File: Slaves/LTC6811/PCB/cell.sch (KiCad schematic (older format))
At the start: 5 parts

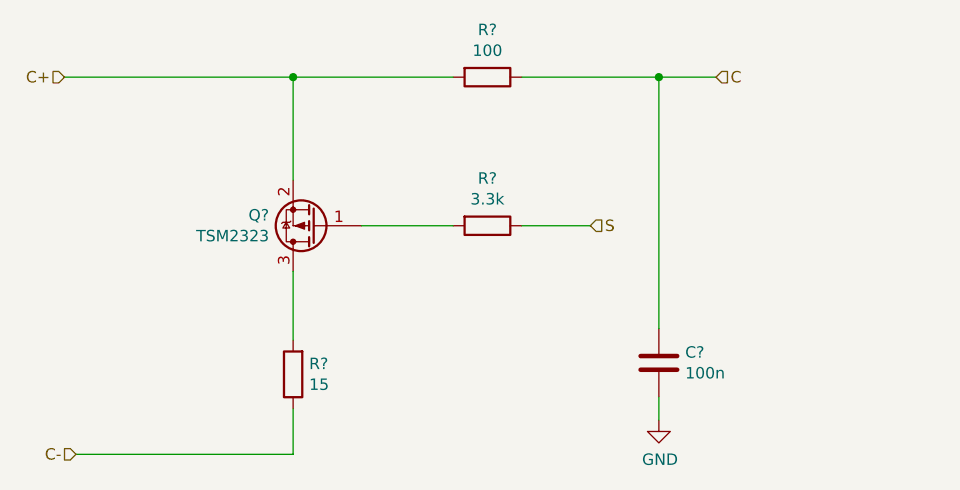
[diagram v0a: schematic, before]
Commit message: LTC6811 PCB completed
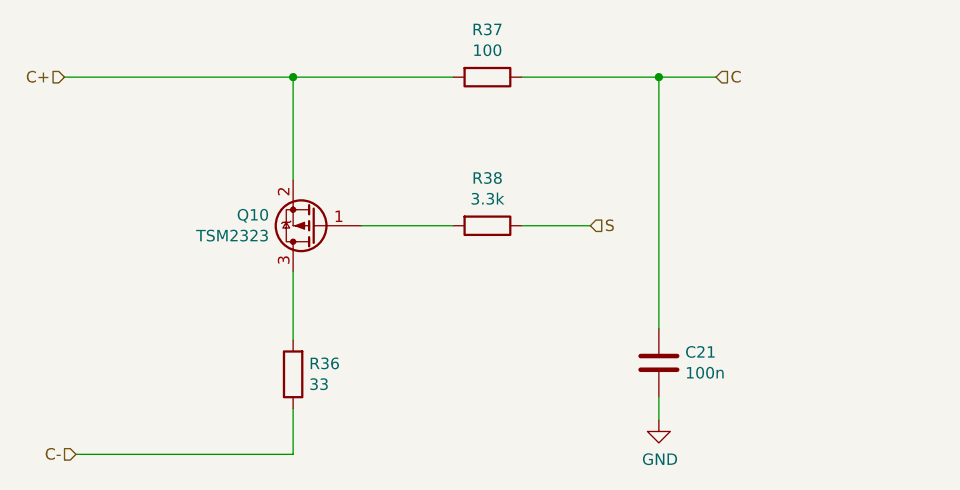
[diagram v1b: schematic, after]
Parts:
- C13: renamed from C?; footprint Capacitors_SMD:C_0805_HandSoldering -> Capacitors_SMD:C_0603_HandSoldering
- R12: renamed from R?; value 15 -> 33; footprint Resistors_SMD:R_2512_HandSoldering -> Resistors_SMD:R_2512
- gave numbers to parts that had none: 3
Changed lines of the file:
@@
 $Descr A4 11693 8268
 encoding utf-8
-Sheet 2 13
+Sheet 10 13
 Title ""
 Date ""
@@
 $EndDescr
 $Comp
-L Device:R R?
+L Device:R R13
 U 1 1 5C4F5B30
 P 4650 2700
-AR Path="/5C4F59F4/5C4F5B30" Ref="R?"  Part="1"
-AR Path="/5C4FCBE0/5C4F5B30" Ref="R?"  Part="1"
-AR Path="/5C4FCED2/5C4F5B30" Ref="R?"  Part="1"
-AR Path="/5C4FCED8/5C4F5B30" Ref="R?"  Part="1"
-AR Path="/5C4FD32A/5C4F5B30" Ref="R?"  Part="1"
-AR Path="/5C4FD330/5C4F5B30" Ref="R?"  Part="1"
-AR Path="/5C4FD336/5C4F5B30" Ref="R?"  Part="1"
-AR Path="/5C4FD33C/5C4F5B30" Ref="R?"  Part="1"
-AR Path="/5C4FFA25/5C4F5B30" Ref="R?"  Part="1"
-AR Path="/5C4FFA2B/5C4F5B30" Ref="R?"  Part="1"
-AR Path="/5C4FFA31/5C4F5B30" Ref="R?"  Part="1"
-AR Path="/5C4FFA37/5C4F5B30" Ref="R?"  Part="1"
+AR Path="/5C4F59F4/5C4F5B30" Ref="R13"  Part="1"
+AR Path="/5C4FCBE0/5C4F5B30" Ref="R16"  Part="1"
+AR Path="/5C4FCED2/5C4F5B30" Ref="R19"  Part="1"
+AR Path="/5C4FCED8/5C4F5B30" Ref="R22"  Part="1"
+AR Path="/5C4FD32A/5C4F5B30" Ref="R25"  Part="1"
+AR Path="/5C4FD330/5C4F5B30" Ref="R28"  Part="1"
+AR Path="/5C4FD336/5C4F5B30" Ref="R31"  Part="1"
+AR Path="/5C4FD33C/5C4F5B30" Ref="R34"  Part="1"
+AR Path="/5C4FFA25/5C4F5B30" Ref="R37"  Part="1"
+AR Path="/5C4FFA2B/5C4F5B30" Ref="R40"  Part="1"
+AR Path="/5C4FFA31/5C4F5B30" Ref="R43"  Part="1"
+AR Path="/5C4FFA37/5C4F5B30" Ref="R46"  Part="1"
 AR Path="/5C4FFA3D/5C4F5B30" Ref="R?"  Part="1"
 AR Path="/5C4FFA43/5C4F5B30" Ref="R?"  Part="1"
-F 0 "R?" V 4443 2700 50  0000 C CNN
+F 0 "R37" V 4443 2700 50  0000 C CNN
 F 1 "100" V 4534 2700 50  0000 C CNN
 F 2 "Resistors_SMD:R_0603_HandSoldering" V 4580 2700 50  0001 C CNN
@@
 $EndComp
 $Comp
-L Device:R R?
+L Device:R R14
 U 1 1 5C4F5DDD
 P 4650 3350
-AR Path="/5C4F59F4/5C4F5DDD" Ref="R?"  Part="1"
-AR Path="/5C4FCBE0/5C4F5DDD" Ref="R?"  Part="1"
-AR Path="/5C4FCED2/5C4F5DDD" Ref="R?"  Part="1"
-AR Path="/5C4FCED8/5C4F5DDD" Ref="R?"  Part="1"
-AR Path="/5C4FD32A/5C4F5DDD" Ref="R?"  Part="1"
-AR Path="/5C4FD330/5C4F5DDD" Ref="R?"  Part="1"
-AR Path="/5C4FD336/5C4F5DDD" Ref="R?"  Part="1"
-AR Path="/5C4FD33C/5C4F5DDD" Ref="R?"  Part="1"
-AR Path="/5C4FFA25/5C4F5DDD" Ref="R?"  Part="1"
-AR Path="/5C4FFA2B/5C4F5DDD" Ref="R?"  Part="1"
-AR Path="/5C4FFA31/5C4F5DDD" Ref="R?"  Part="1"
-AR Path="/5C4FFA37/5C4F5DDD" Ref="R?"  Part="1"
+AR Path="/5C4F59F4/5C4F5DDD" Ref="R14"  Part="1"
+AR Path="/5C4FCBE0/5C4F5DDD" Ref="R17"  Part="1"
+AR Path="/5C4FCED2/5C4F5DDD" Ref="R20"  Part="1"
+AR Path="/5C4FCED8/5C4F5DDD" Ref="R23"  Part="1"
+AR Path="/5C4FD32A/5C4F5DDD" Ref="R26"  Part="1"
+AR Path="/5C4FD330/5C4F5DDD" Ref="R29"  Part="1"
+AR Path="/5C4FD336/5C4F5DDD" Ref="R32"  Part="1"
+AR Path="/5C4FD33C/5C4F5DDD" Ref="R35"  Part="1"
+AR Path="/5C4FFA25/5C4F5DDD" Ref="R38"  Part="1"
+AR Path="/5C4FFA2B/5C4F5DDD" Ref="R41"  Part="1"
+AR Path="/5C4FFA31/5C4F5DDD" Ref="R44"  Part="1"
+AR Path="/5C4FFA37/5C4F5DDD" Ref="R47"  Part="1"
 AR Path="/5C4FFA3D/5C4F5DDD" Ref="R?"  Part="1"
 AR Path="/5C4FFA43/5C4F5DDD" Ref="R?"  Part="1"
-F 0 "R?" V 4443 3350 50  0000 C CNN
+F 0 "R38" V 4443 3350 50  0000 C CNN
 F 1 "3.3k" V 4534 3350 50  0000 C CNN
 F 2 "Resistors_SMD:R_0603_HandSoldering" V 4580 3350 50  0001 C CNN
@@
 $EndComp
 $Comp
-L Device:Q_PMOS_GSD Q?
+L Device:Q_PMOS_GSD Q2
 U 1 1 5C4F756B
 P 3900 3350
-AR Path="/5C4F59F4/5C4F756B" Ref="Q?"  Part="1"
-AR Path="/5C4FCBE0/5C4F756B" Ref="Q?"  Part="1"
-AR Path="/5C4FCED2/5C4F756B" Ref="Q?"  Part="1"
-AR Path="/5C4FCED8/5C4F756B" Ref="Q?"  Part="1"
-AR Path="/5C4FD32A/5C4F756B" Ref="Q?"  Part="1"
-AR Path="/5C4FD330/5C4F756B" Ref="Q?"  Part="1"
-AR Path="/5C4FD336/5C4F756B" Ref="Q?"  Part="1"
-AR Path="/5C4FD33C/5C4F756B" Ref="Q?"  Part="1"
-AR Path="/5C4FFA25/5C4F756B" Ref="Q?"  Part="1"
-AR Path="/5C4FFA2B/5C4F756B" Ref="Q?"  Part="1"
-AR Path="/5C4FFA31/5C4F756B" Ref="Q?"  Part="1"
-AR Path="/5C4FFA37/5C4F756B" Ref="Q?"  Part="1"
+AR Path="/5C4F59F4/5C4F756B" Ref="Q2"  Part="1"
+AR Path="/5C4FCBE0/5C4F756B" Ref="Q3"  Part="1"
+AR Path="/5C4FCED2/5C4F756B" Ref="Q4"  Part="1"
+AR Path="/5C4FCED8/5C4F756B" Ref="Q5"  Part="1"
+AR Path="/5C4FD32A/5C4F756B" Ref="Q6"  Part="1"
+AR Path="/5C4FD330/5C4F756B" Ref="Q7"  Part="1"
+AR Path="/5C4FD336/5C4F756B" Ref="Q8"  Part="1"
+AR Path="/5C4FD33C/5C4F756B" Ref="Q9"  Part="1"
+AR Path="/5C4FFA25/5C4F756B" Ref="Q10"  Part="1"
+AR Path="/5C4FFA2B/5C4F756B" Ref="Q11"  Part="1"
+AR Path="/5C4FFA31/5C4F756B" Ref="Q12"  Part="1"
+AR Path="/5C4FFA37/5C4F756B" Ref="Q13"  Part="1"
 AR Path="/5C4FFA3D/5C4F756B" Ref="Q?"  Part="1"
 AR Path="/5C4FFA43/5C4F756B" Ref="Q?"  Part="1"
-F 0 "Q?" H 4105 3304 50  0000 L CNN
+F 0 "Q10" H 4105 3304 50  0000 L CNN
 F 1 "TSM2323" H 4105 3395 50  0000 L CNN
 F 2 "TO_SOT_Packages_SMD:SOT-23" H 4100 3450 50  0001 C CNN
@@
 	3800 2700 3800 3150
 $Comp
-L Device:R R?
+L Device:R R12
 U 1 1 5C4F932B
 P 3800 4000
-AR Path="/5C4F59F4/5C4F932B" Ref="R?"  Part="1"
-AR Path="/5C4FCBE0/5C4F932B" Ref="R?"  Part="1"
-AR Path="/5C4FCED2/5C4F932B" Ref="R?"  Part="1"
-AR Path="/5C4FCED8/5C4F932B" Ref="R?"  Part="1"
-AR Path="/5C4FD32A/5C4F932B" Ref="R?"  Part="1"
-AR Path="/5C4FD330/5C4F932B" Ref="R?"  Part="1"
-AR Path="/5C4FD336/5C4F932B" Ref="R?"  Part="1"
-AR Path="/5C4FD33C/5C4F932B" Ref="R?"  Part="1"
-AR Path="/5C4FFA25/5C4F932B" Ref="R?"  Part="1"
-AR Path="/5C4FFA2B/5C4F932B" Ref="R?"  Part="1"
-AR Path="/5C4FFA31/5C4F932B" Ref="R?"  Part="1"
-AR Path="/5C4FFA37/5C4F932B" Ref="R?"  Part="1"
+AR Path="/5C4F59F4/5C4F932B" Ref="R12"  Part="1"
+AR Path="/5C4FCBE0/5C4F932B" Ref="R15"  Part="1"
+AR Path="/5C4FCED2/5C4F932B" Ref="R18"  Part="1"
+AR Path="/5C4FCED8/5C4F932B" Ref="R21"  Part="1"
+AR Path="/5C4FD32A/5C4F932B" Ref="R24"  Part="1"
+AR Path="/5C4FD330/5C4F932B" Ref="R27"  Part="1"
+AR Path="/5C4FD336/5C4F932B" Ref="R30"  Part="1"
+AR Path="/5C4FD33C/5C4F932B" Ref="R33"  Part="1"
+AR Path="/5C4FFA25/5C4F932B" Ref="R36"  Part="1"
+AR Path="/5C4FFA2B/5C4F932B" Ref="R39"  Part="1"
+AR Path="/5C4FFA31/5C4F932B" Ref="R42"  Part="1"
+AR Path="/5C4FFA37/5C4F932B" Ref="R45"  Part="1"
 AR Path="/5C4FFA3D/5C4F932B" Ref="R?"  Part="1"
 AR Path="/5C4FFA43/5C4F932B" Ref="R?"  Part="1"
-F 0 "R?" H 3730 3954 50  0000 R CNN
-F 1 "15" H 3730 4045 50  0000 R CNN
-F 2 "Resistors_SMD:R_2512_HandSoldering" V 3730 4000 50  0001 C CNN
+F 0 "R36" H 3730 3954 50  0000 R CNN
+F 1 "33" H 3730 4045 50  0000 R CNN
+F 2 "Resistors_SMD:R_2512" V 3730 4000 50  0001 C CNN
 F 3 "~" H 3800 4000 50  0001 C CNN
 	1    3800 4000
@@
 	5400 2700 5650 2700
 $Comp
-L Device:C C?
+L Device:C C13
 U 1 1 5C4F9945
 P 5400 3950
-AR Path="/5C4F59F4/5C4F9945" Ref="C?"  Part="1"
-AR Path="/5C4FCBE0/5C4F9945" Ref="C?"  Part="1"
-AR Path="/5C4FCED2/5C4F9945" Ref="C?"  Part="1"
-AR Path="/5C4FCED8/5C4F9945" Ref="C?"  Part="1"
-AR Path="/5C4FD32A/5C4F9945" Ref="C?"  Part="1"
-AR Path="/5C4FD330/5C4F9945" Ref="C?"  Part="1"
-AR Path="/5C4FD336/5C4F9945" Ref="C?"  Part="1"
-AR Path="/5C4FD33C/5C4F9945" Ref="C?"  Part="1"
-AR Path="/5C4FFA25/5C4F9945" Ref="C?"  Part="1"
-AR Path="/5C4FFA2B/5C4F9945" Ref="C?"  Part="1"
-AR Path="/5C4FFA31/5C4F9945" Ref="C?"  Part="1"
-AR Path="/5C4FFA37/5C4F9945" Ref="C?"  Part="1"
+AR Path="/5C4F59F4/5C4F9945" Ref="C13"  Part="1"
+AR Path="/5C4FCBE0/5C4F9945" Ref="C14"  Part="1"
+AR Path="/5C4FCED2/5C4F9945" Ref="C15"  Part="1"
+AR Path="/5C4FCED8/5C4F9945" Ref="C16"  Part="1"
+AR Path="/5C4FD32A/5C4F9945" Ref="C17"  Part="1"
+AR Path="/5C4FD330/5C4F9945" Ref="C18"  Part="1"
+AR Path="/5C4FD336/5C4F9945" Ref="C19"  Part="1"
+AR Path="/5C4FD33C/5C4F9945" Ref="C20"  Part="1"
+AR Path="/5C4FFA25/5C4F9945" Ref="C21"  Part="1"
+AR Path="/5C4FFA2B/5C4F9945" Ref="C22"  Part="1"
+AR Path="/5C4FFA31/5C4F9945" Ref="C23"  Part="1"
+AR Path="/5C4FFA37/5C4F9945" Ref="C24"  Part="1"
 AR Path="/5C4FFA3D/5C4F9945" Ref="C?"  Part="1"
 AR Path="/5C4FFA43/5C4F9945" Ref="C?"  Part="1"
-F 0 "C?" H 5515 3996 50  0000 L CNN
+F 0 "C21" H 5515 3996 50  0000 L CNN
 F 1 "100n" H 5515 3905 50  0000 L CNN
-F 2 "Capacitors_SMD:C_0805_HandSoldering" H 5438 3800 50  0001 C CNN
+F 2 "Capacitors_SMD:C_0603_HandSoldering" H 5438 3800 50  0001 C CNN
 F 3 "~" H 5400 3950 50  0001 C CNN
 	1    5400 3950
@@
 $EndComp
 $Comp
-L power:GND #PWR?
+L power:GND #PWR0109
 U 1 1 5C4FAC2C
 P 5400 4200
-AR Path="/5C4F59F4/5C4FAC2C" Ref="#PWR?"  Part="1"
-AR Path="/5C4FCBE0/5C4FAC2C" Ref="#PWR?"  Part="1"
-AR Path="/5C4FCED2/5C4FAC2C" Ref="#PWR?"  Part="1"
-AR Path="/5C4FCED8/5C4FAC2C" Ref="#PWR?"  Part="1"
-AR Path="/5C4FD32A/5C4FAC2C" Ref="#PWR?"  Part="1"
-AR Path="/5C4FD330/5C4FAC2C" Ref="#PWR?"  Part="1"
-AR Path="/5C4FD336/5C4FAC2C" Ref="#PWR?"  Part="1"
-AR Path="/5C4FD33C/5C4FAC2C" Ref="#PWR?"  Part="1"
-AR Path="/5C4FFA25/5C4FAC2C" Ref="#PWR?"  Part="1"
-AR Path="/5C4FFA2B/5C4FAC2C" Ref="#PWR?"  Part="1"
-AR Path="/5C4FFA31/5C4FAC2C" Ref="#PWR?"  Part="1"
-AR Path="/5C4FFA37/5C4FAC2C" Ref="#PWR?"  Part="1"
+AR Path="/5C4F59F4/5C4FAC2C" Ref="#PWR0109"  Part="1"
+AR Path="/5C4FCBE0/5C4FAC2C" Ref="#PWR0110"  Part="1"
+AR Path="/5C4FCED2/5C4FAC2C" Ref="#PWR0111"  Part="1"
+AR Path="/5C4FCED8/5C4FAC2C" Ref="#PWR0112"  Part="1"
+AR Path="/5C4FD32A/5C4FAC2C" Ref="#PWR0113"  Part="1"
+AR Path="/5C4FD330/5C4FAC2C" Ref="#PWR0114"  Part="1"
+AR Path="/5C4FD336/5C4FAC2C" Ref="#PWR0115"  Part="1"
+AR Path="/5C4FD33C/5C4FAC2C" Ref="#PWR0116"  Part="1"
+AR Path="/5C4FFA25/5C4FAC2C" Ref="#PWR0117"  Part="1"
+AR Path="/5C4FFA2B/5C4FAC2C" Ref="#PWR0118"  Part="1"
+AR Path="/5C4FFA31/5C4FAC2C" Ref="#PWR0119"  Part="1"
+AR Path="/5C4FFA37/5C4FAC2C" Ref="#PWR0120"  Part="1"
 AR Path="/5C4FFA3D/5C4FAC2C" Ref="#PWR?"  Part="1"
 AR Path="/5C4FFA43/5C4FAC2C" Ref="#PWR?"  Part="1"
-F 0 "#PWR?" H 5400 3950 50  0001 C CNN
+F 0 "#PWR0117" H 5400 3950 50  0001 C CNN
 F 1 "GND" H 5405 4027 50  0000 C CNN
 F 2 "" H 5400 4200 50  0001 C CNN

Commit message: description on PCB
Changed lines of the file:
@@
 AR Path="/5C4FFA3D/5C4F5B30" Ref="R?"  Part="1"
 AR Path="/5C4FFA43/5C4F5B30" Ref="R?"  Part="1"
-F 0 "R37" V 4443 2700 50  0000 C CNN
+F 0 "R46" V 4443 2700 50  0000 C CNN
 F 1 "100" V 4534 2700 50  0000 C CNN
 F 2 "Resistors_SMD:R_0603_HandSoldering" V 4580 2700 50  0001 C CNN
@@
 AR Path="/5C4FFA3D/5C4F5DDD" Ref="R?"  Part="1"
 AR Path="/5C4FFA43/5C4F5DDD" Ref="R?"  Part="1"
-F 0 "R38" V 4443 3350 50  0000 C CNN
+F 0 "R47" V 4443 3350 50  0000 C CNN
 F 1 "3.3k" V 4534 3350 50  0000 C CNN
 F 2 "Resistors_SMD:R_0603_HandSoldering" V 4580 3350 50  0001 C CNN
@@
 AR Path="/5C4FFA3D/5C4F756B" Ref="Q?"  Part="1"
 AR Path="/5C4FFA43/5C4F756B" Ref="Q?"  Part="1"
-F 0 "Q10" H 4105 3304 50  0000 L CNN
+F 0 "Q13" H 4105 3304 50  0000 L CNN
 F 1 "TSM2323" H 4105 3395 50  0000 L CNN
 F 2 "TO_SOT_Packages_SMD:SOT-23" H 4100 3450 50  0001 C CNN
@@
 AR Path="/5C4FFA3D/5C4F932B" Ref="R?"  Part="1"
 AR Path="/5C4FFA43/5C4F932B" Ref="R?"  Part="1"
-F 0 "R36" H 3730 3954 50  0000 R CNN
+F 0 "R45" H 3730 3954 50  0000 R CNN
 F 1 "33" H 3730 4045 50  0000 R CNN
 F 2 "Resistors_SMD:R_2512" V 3730 4000 50  0001 C CNN
@@
 AR Path="/5C4FFA3D/5C4F9945" Ref="C?"  Part="1"
 AR Path="/5C4FFA43/5C4F9945" Ref="C?"  Part="1"
-F 0 "C21" H 5515 3996 50  0000 L CNN
+F 0 "C24" H 5515 3996 50  0000 L CNN
 F 1 "100n" H 5515 3905 50  0000 L CNN
 F 2 "Capacitors_SMD:C_0603_HandSoldering" H 5438 3800 50  0001 C CNN
@@
 AR Path="/5C4FFA3D/5C4FAC2C" Ref="#PWR?"  Part="1"
 AR Path="/5C4FFA43/5C4FAC2C" Ref="#PWR?"  Part="1"
-F 0 "#PWR0117" H 5400 3950 50  0001 C CNN
+F 0 "#PWR0120" H 5400 3950 50  0001 C CNN
 F 1 "GND" H 5405 4027 50  0000 C CNN
 F 2 "" H 5400 4200 50  0001 C CNN

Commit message: gerbers
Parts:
- C13: footprint Capacitors_SMD:C_0603_HandSoldering -> Capacitors_SMD:C_0805_HandSoldering
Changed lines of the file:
@@
 $Descr A4 11693 8268
 encoding utf-8
-Sheet 10 13
+Sheet 2 13
 Title ""
 Date ""
@@
 AR Path="/5C4FFA3D/5C4F5B30" Ref="R?"  Part="1"
 AR Path="/5C4FFA43/5C4F5B30" Ref="R?"  Part="1"
-F 0 "R46" V 4443 2700 50  0000 C CNN
+F 0 "R13" V 4443 2700 50  0000 C CNN
 F 1 "100" V 4534 2700 50  0000 C CNN
 F 2 "Resistors_SMD:R_0603_HandSoldering" V 4580 2700 50  0001 C CNN
@@
 AR Path="/5C4FFA3D/5C4F5DDD" Ref="R?"  Part="1"
 AR Path="/5C4FFA43/5C4F5DDD" Ref="R?"  Part="1"
-F 0 "R47" V 4443 3350 50  0000 C CNN
+F 0 "R14" V 4443 3350 50  0000 C CNN
 F 1 "3.3k" V 4534 3350 50  0000 C CNN
 F 2 "Resistors_SMD:R_0603_HandSoldering" V 4580 3350 50  0001 C CNN
@@
 AR Path="/5C4FFA3D/5C4F756B" Ref="Q?"  Part="1"
 AR Path="/5C4FFA43/5C4F756B" Ref="Q?"  Part="1"
-F 0 "Q13" H 4105 3304 50  0000 L CNN
+F 0 "Q2" H 4105 3304 50  0000 L CNN
 F 1 "TSM2323" H 4105 3395 50  0000 L CNN
 F 2 "TO_SOT_Packages_SMD:SOT-23" H 4100 3450 50  0001 C CNN
@@
 AR Path="/5C4FFA3D/5C4F932B" Ref="R?"  Part="1"
 AR Path="/5C4FFA43/5C4F932B" Ref="R?"  Part="1"
-F 0 "R45" H 3730 3954 50  0000 R CNN
+F 0 "R12" H 3730 3954 50  0000 R CNN
 F 1 "33" H 3730 4045 50  0000 R CNN
 F 2 "Resistors_SMD:R_2512" V 3730 4000 50  0001 C CNN
@@
 AR Path="/5C4FFA3D/5C4F9945" Ref="C?"  Part="1"
 AR Path="/5C4FFA43/5C4F9945" Ref="C?"  Part="1"
-F 0 "C24" H 5515 3996 50  0000 L CNN
+F 0 "C13" H 5515 3996 50  0000 L CNN
 F 1 "100n" H 5515 3905 50  0000 L CNN
-F 2 "Capacitors_SMD:C_0603_HandSoldering" H 5438 3800 50  0001 C CNN
+F 2 "Capacitors_SMD:C_0805_HandSoldering" H 5438 3800 50  0001 C CNN
 F 3 "~" H 5400 3950 50  0001 C CNN
 	1    5400 3950
@@
 AR Path="/5C4FFA3D/5C4FAC2C" Ref="#PWR?"  Part="1"
 AR Path="/5C4FFA43/5C4FAC2C" Ref="#PWR?"  Part="1"
-F 0 "#PWR0120" H 5400 3950 50  0001 C CNN
+F 0 "#PWR0109" H 5400 3950 50  0001 C CNN
 F 1 "GND" H 5405 4027 50  0000 C CNN
 F 2 "" H 5400 4200 50  0001 C CNN

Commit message: Software added
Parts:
- added D?: PDZ7.5B, symbol Device:D_Zener
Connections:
- net C: now also D?.1 (K)
- new net CM: D?.2 (A)
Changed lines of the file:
@@
 Wire Wire Line
 	4800 3350 5100 3350
-Text HLabel 5650 2700 2    50   Input ~ 0
+Text HLabel 6500 2700 2    50   Input ~ 0
 C
 Wire Wire Line
@@
 Connection ~ 5400 2700
 Wire Wire Line
-	5400 2700 5650 2700
+	5400 2700 6000 2700
 $Comp
 L Device:C C13
@@
 Wire Wire Line
 	3800 4350 2850 4350
+$Comp
+L Device:D_Zener D?
+U 1 1 5C7C1653
+P 6000 3300
+AR Path="/5C4F59F4/5C7C1653" Ref="D?"  Part="1"
+AR Path="/5C4FCED2/5C7C1653" Ref="D?"  Part="1"
+F 0 "D?" V 5954 3379 50  0000 L CNN
+F 1 "PDZ7.5B" V 6045 3379 50  0000 L CNN
+F 2 "" H 6000 3300 50  0001 C CNN
+F 3 "~" H 6000 3300 50  0001 C CNN
+	1    6000 3300
+	0    1    1    0
+$EndComp
+Text HLabel 6250 4250 2    50   Input ~ 0
+CM
+Wire Wire Line
+	6000 3150 6000 2700
+Connection ~ 6000 2700
+Wire Wire Line
+	6000 2700 6500 2700
+Wire Wire Line
+	6000 3450 6000 4250
+Wire Wire Line
+	6000 4250 6250 4250
 $EndSCHEMATC

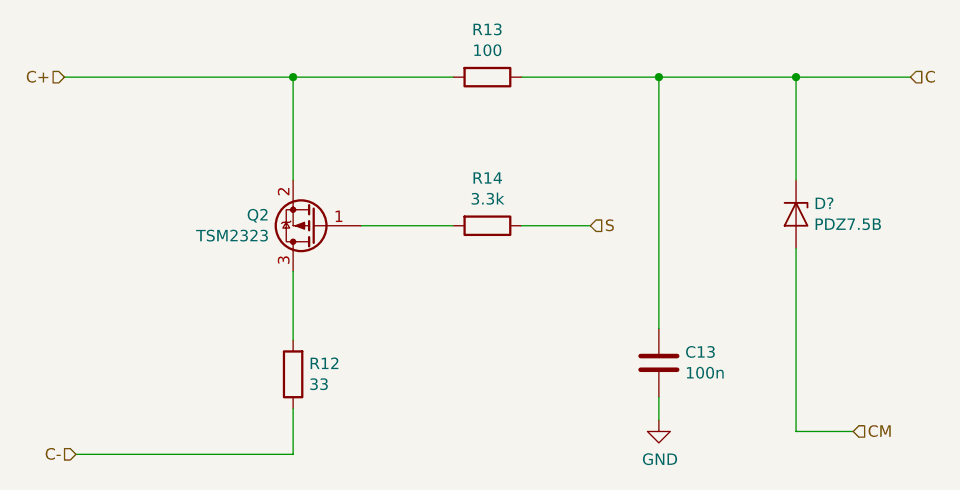
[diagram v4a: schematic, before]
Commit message: LTC6811 added diode protection inputs
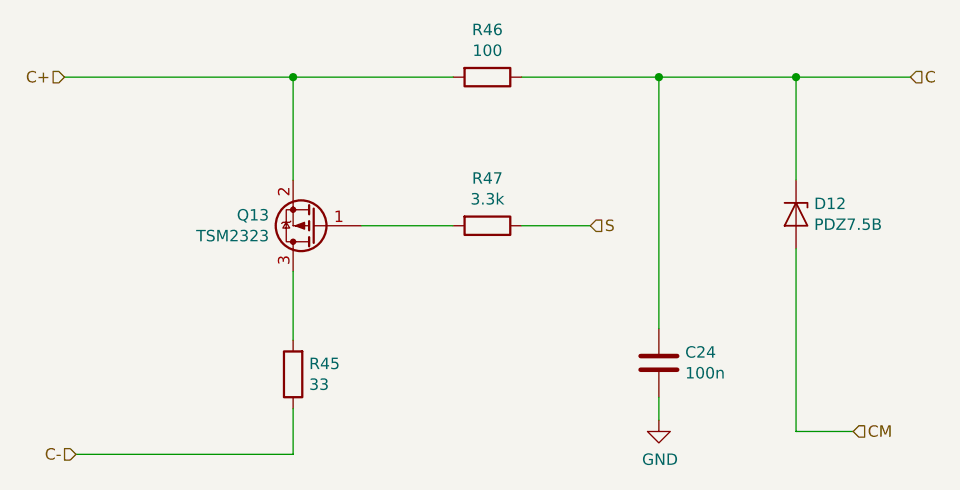
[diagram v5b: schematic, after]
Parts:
- D1: renamed from D?; footprint (none) -> Diodes_SMD:D_SOD-323_HandSoldering
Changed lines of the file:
@@
 $Descr A4 11693 8268
 encoding utf-8
-Sheet 2 13
+Sheet 13 13
 Title ""
 Date ""
@@
 AR Path="/5C4FFA3D/5C4F5B30" Ref="R?"  Part="1"
 AR Path="/5C4FFA43/5C4F5B30" Ref="R?"  Part="1"
-F 0 "R13" V 4443 2700 50  0000 C CNN
+F 0 "R46" V 4443 2700 50  0000 C CNN
 F 1 "100" V 4534 2700 50  0000 C CNN
 F 2 "Resistors_SMD:R_0603_HandSoldering" V 4580 2700 50  0001 C CNN
@@
 AR Path="/5C4FFA3D/5C4F5DDD" Ref="R?"  Part="1"
 AR Path="/5C4FFA43/5C4F5DDD" Ref="R?"  Part="1"
-F 0 "R14" V 4443 3350 50  0000 C CNN
+F 0 "R47" V 4443 3350 50  0000 C CNN
 F 1 "3.3k" V 4534 3350 50  0000 C CNN
 F 2 "Resistors_SMD:R_0603_HandSoldering" V 4580 3350 50  0001 C CNN
@@
 AR Path="/5C4FFA3D/5C4F756B" Ref="Q?"  Part="1"
 AR Path="/5C4FFA43/5C4F756B" Ref="Q?"  Part="1"
-F 0 "Q2" H 4105 3304 50  0000 L CNN
+F 0 "Q13" H 4105 3304 50  0000 L CNN
 F 1 "TSM2323" H 4105 3395 50  0000 L CNN
 F 2 "TO_SOT_Packages_SMD:SOT-23" H 4100 3450 50  0001 C CNN
@@
 AR Path="/5C4FFA3D/5C4F932B" Ref="R?"  Part="1"
 AR Path="/5C4FFA43/5C4F932B" Ref="R?"  Part="1"
-F 0 "R12" H 3730 3954 50  0000 R CNN
+F 0 "R45" H 3730 3954 50  0000 R CNN
 F 1 "33" H 3730 4045 50  0000 R CNN
 F 2 "Resistors_SMD:R_2512" V 3730 4000 50  0001 C CNN
@@
 AR Path="/5C4FFA3D/5C4F9945" Ref="C?"  Part="1"
 AR Path="/5C4FFA43/5C4F9945" Ref="C?"  Part="1"
-F 0 "C13" H 5515 3996 50  0000 L CNN
+F 0 "C24" H 5515 3996 50  0000 L CNN
 F 1 "100n" H 5515 3905 50  0000 L CNN
 F 2 "Capacitors_SMD:C_0805_HandSoldering" H 5438 3800 50  0001 C CNN
@@
 AR Path="/5C4FFA3D/5C4FAC2C" Ref="#PWR?"  Part="1"
 AR Path="/5C4FFA43/5C4FAC2C" Ref="#PWR?"  Part="1"
-F 0 "#PWR0109" H 5400 3950 50  0001 C CNN
+F 0 "#PWR0120" H 5400 3950 50  0001 C CNN
 F 1 "GND" H 5405 4027 50  0000 C CNN
 F 2 "" H 5400 4200 50  0001 C CNN
@@
 	3800 4350 2850 4350
 $Comp
-L Device:D_Zener D?
+L Device:D_Zener D1
 U 1 1 5C7C1653
 P 6000 3300
-AR Path="/5C4F59F4/5C7C1653" Ref="D?"  Part="1"
-AR Path="/5C4FCED2/5C7C1653" Ref="D?"  Part="1"
-F 0 "D?" V 5954 3379 50  0000 L CNN
+AR Path="/5C4F59F4/5C7C1653" Ref="D1"  Part="1"
+AR Path="/5C4FCED2/5C7C1653" Ref="D3"  Part="1"
+AR Path="/5C4FCBE0/5C7C1653" Ref="D2"  Part="1"
+AR Path="/5C4FCED8/5C7C1653" Ref="D4"  Part="1"
+AR Path="/5C4FD32A/5C7C1653" Ref="D5"  Part="1"
+AR Path="/5C4FD330/5C7C1653" Ref="D6"  Part="1"
+AR Path="/5C4FD336/5C7C1653" Ref="D7"  Part="1"
+AR Path="/5C4FD33C/5C7C1653" Ref="D8"  Part="1"
+AR Path="/5C4FFA25/5C7C1653" Ref="D9"  Part="1"
+AR Path="/5C4FFA2B/5C7C1653" Ref="D10"  Part="1"
+AR Path="/5C4FFA31/5C7C1653" Ref="D11"  Part="1"
+AR Path="/5C4FFA37/5C7C1653" Ref="D12"  Part="1"
+F 0 "D12" V 5954 3379 50  0000 L CNN
 F 1 "PDZ7.5B" V 6045 3379 50  0000 L CNN
-F 2 "" H 6000 3300 50  0001 C CNN
+F 2 "Diodes_SMD:D_SOD-323_HandSoldering" H 6000 3300 50  0001 C CNN
 F 3 "~" H 6000 3300 50  0001 C CNN
 	1    6000 3300
